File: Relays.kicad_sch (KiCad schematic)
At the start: 17 parts, among them J28 1862424, J29 1862424, J30 1862424, J31 1862424, J32 1862424, J33 1862424, J34 1862424, J35 1862424, K1 G5LE-1, K2 G5LE-1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

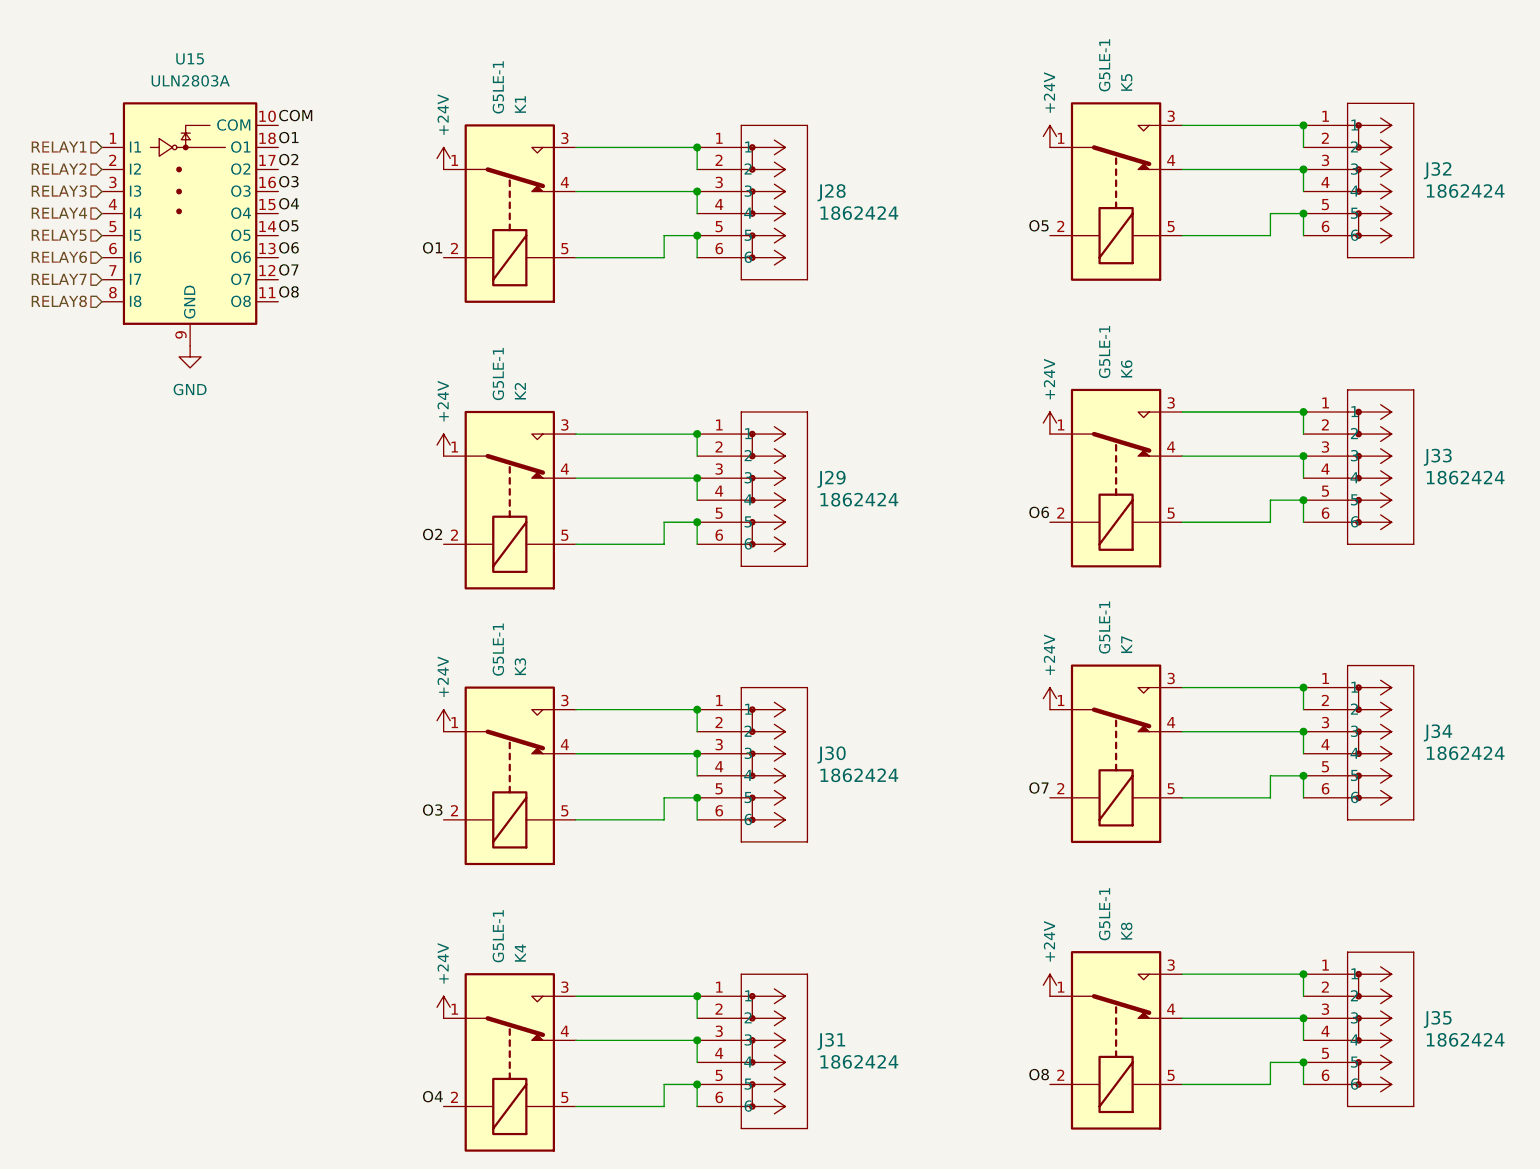
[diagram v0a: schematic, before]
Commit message: Updated schematic and PCB
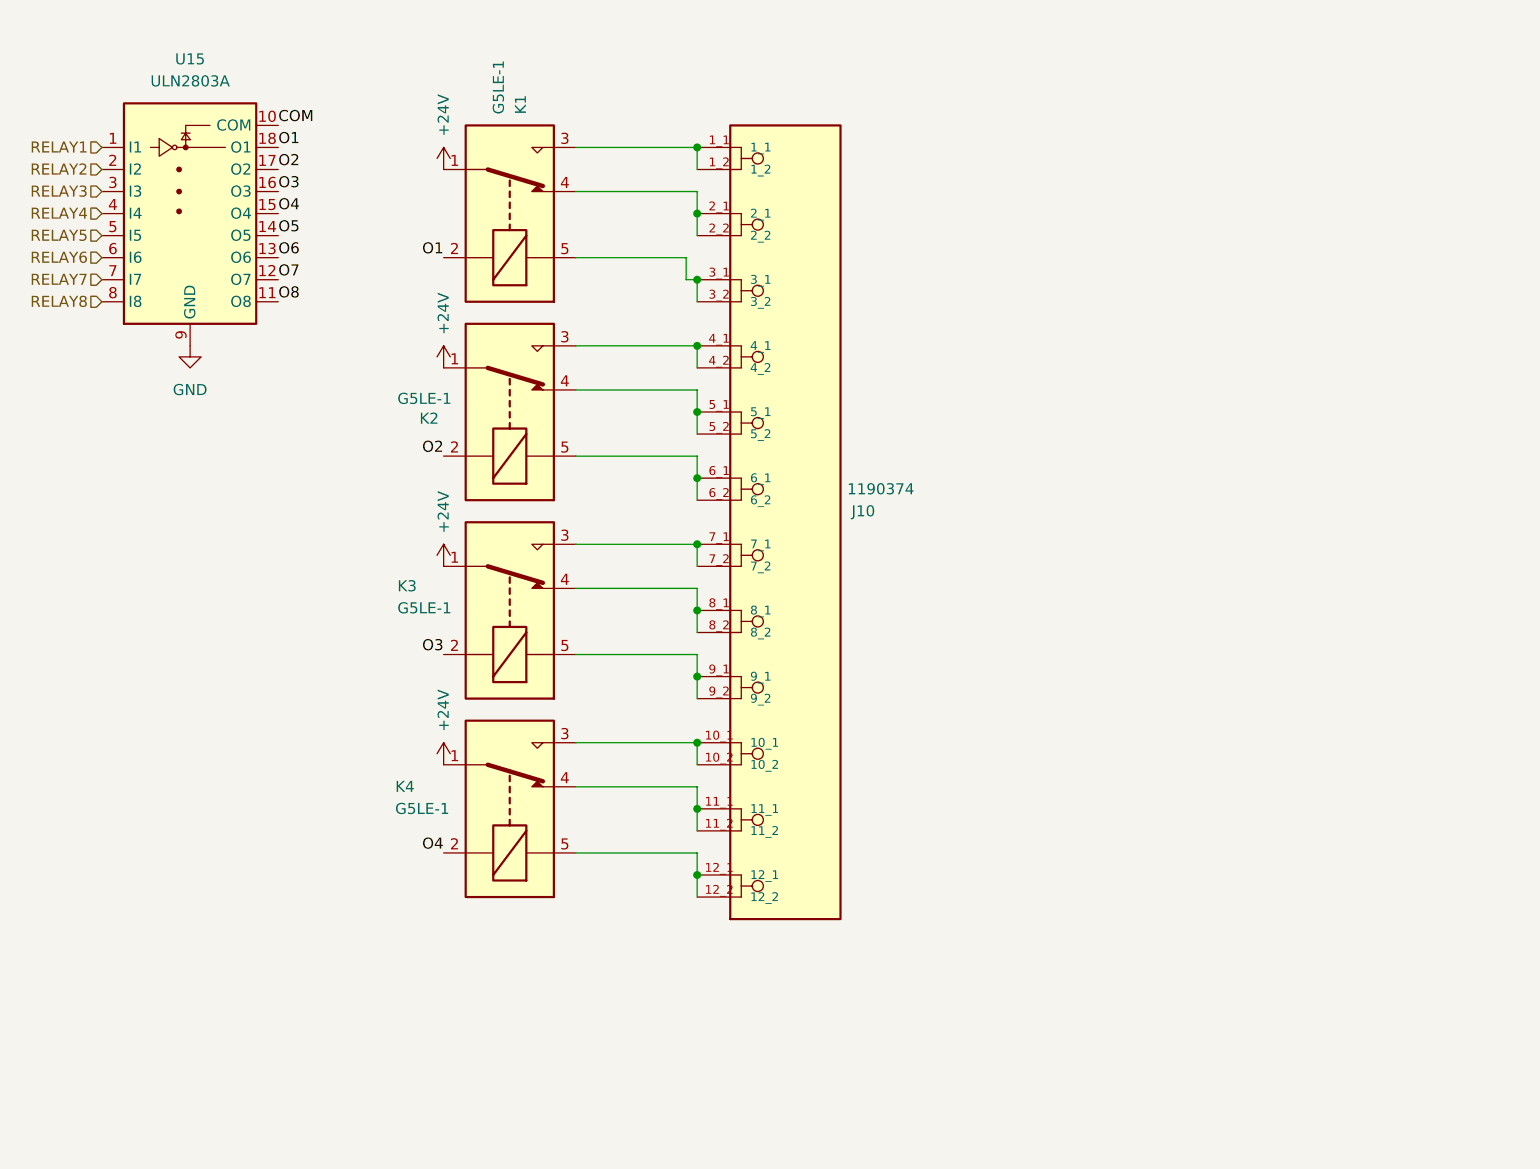
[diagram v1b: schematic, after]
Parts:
- removed J28, J29, J30, J31, J32, J33, J34, J35: 1862424, CONN_1862424, symbol 2026-03-28_19-29-49:1862424
- removed K5, K6, K7, K8: G5LE-1, Relay_THT:Relay_SPDT_Omron-G5LE-1, symbol Relay:G5LE-1
- added J10: 1190374, LPTA 2,512-5,0 - PCB terminal block1:PHOENIX_1190374, symbol 1190374:1190374
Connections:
- net at K2.3: now also J10.4_1, J10.4_2
- net at K2.4: now also J10.5_1, J10.5_2
- net at K2.5: now also J10.6_1, J10.6_2
- net at K3.3: now also J10.7_1, J10.7_2
- net at K3.4: now also J10.8_1, J10.8_2
- net at K3.5: now also J10.9_1, J10.9_2
- net at K4.3: now also J10.10_1, J10.10_2
- net at K4.4: now also J10.11_1, J10.11_2
- net at K4.5: now also J10.12_1, J10.12_2
- net at K1.3: now also J10.1_1, J10.1_2
- net at K1.4: now also J10.2_1, J10.2_2
- net at K1.5: now also J10.3_1, J10.3_2
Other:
- moved on the sheet: K2, K3, K4
